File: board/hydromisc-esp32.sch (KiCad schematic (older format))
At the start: 53 parts, among them CN12 MOLEX_2x3, CN13 MOLEX_2x3, CN14 COAX_CONNECTOR, CN15 HEADER_6, CN16 MOLEX_2x2, CN3 COAX_CONNECTOR, CN4 MOLEX_2x2, IC2 74HC594, IC4 74HC594, IC5 opamp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

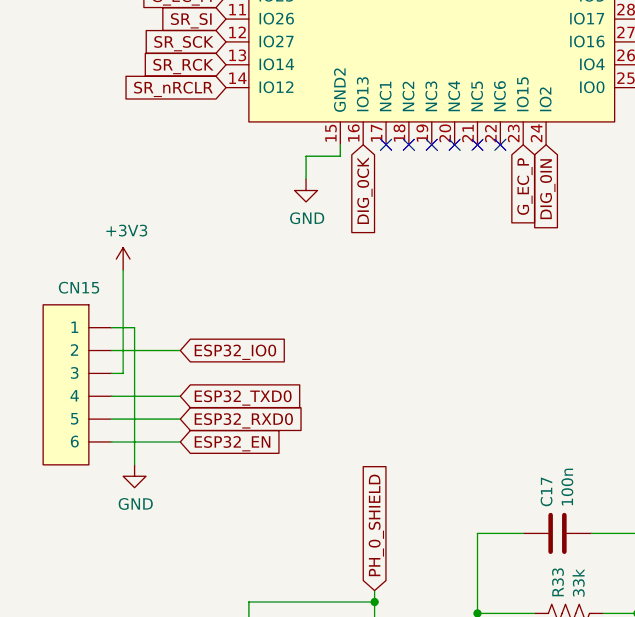
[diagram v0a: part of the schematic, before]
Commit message: Update PCB to rev B.
Add the missing pull-up on ESP32_EN, some pull-down on Vuser to
fight off-brand LM2596 leakage current, and a README.md explaining.
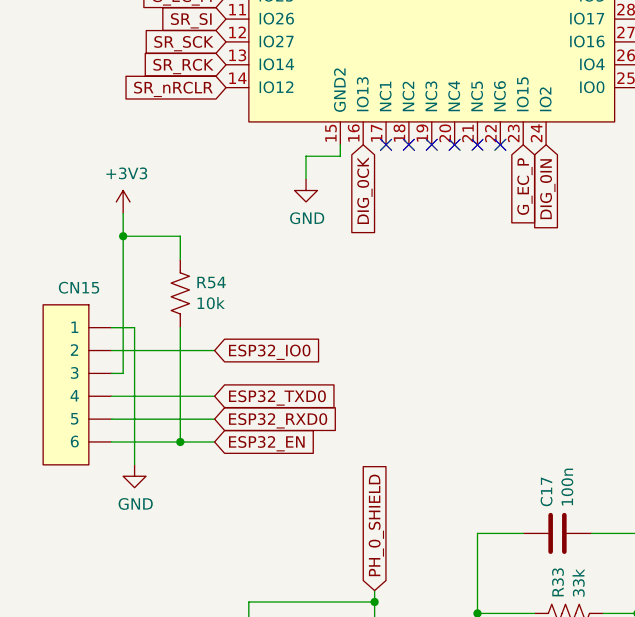
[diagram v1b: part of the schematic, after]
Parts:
- added R54: 10k, hydromisc:HM_0603, symbol Device:R_US
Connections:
- net +3V3: now also R54.1
- net ESP32_EN: now also R54.2
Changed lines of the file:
@@
 Wire Wire Line
 	1300 4100 1350 4100
-Wire Wire Line
-	1350 4100 1350 3650
 $Comp
 L power:+3V3 #PWR0125
 U 1 1 6114B426
-P 1350 3650
-F 0 "#PWR0125" H 1350 3500 50  0001 C CNN
-F 1 "+3V3" H 1365 3823 50  0000 C CNN
-F 2 "" H 1350 3650 50  0001 C CNN
-F 3 "" H 1350 3650 50  0001 C CNN
-	1    1350 3650
-	1    0    0    -1
-$EndComp
-Wire Wire Line
-	1600 4000 1300 4000
-Wire Wire Line
-	1600 4200 1300 4200
-Wire Wire Line
-	1600 4300 1300 4300
-Wire Wire Line
-	1600 4400 1300 4400
-Text GLabel 1600 4000 2    50   Input ~ 0
+P 1350 3400
+F 0 "#PWR0125" H 1350 3250 50  0001 C CNN
+F 1 "+3V3" H 1365 3573 50  0000 C CNN
+F 2 "" H 1350 3400 50  0001 C CNN
+F 3 "" H 1350 3400 50  0001 C CNN
+	1    1350 3400
+	1    0    0    -1
+$EndComp
+Text GLabel 1750 4000 2    50   Input ~ 0
 ESP32_IO0
-Text GLabel 1600 4200 2    50   Input ~ 0
+Text GLabel 1750 4200 2    50   Input ~ 0
 ESP32_TXD0
-Text GLabel 1600 4300 2    50   Input ~ 0
+Text GLabel 1750 4300 2    50   Input ~ 0
 ESP32_RXD0
-Text GLabel 1600 4400 2    50   Input ~ 0
+Text GLabel 1750 4400 2    50   Input ~ 0
 ESP32_EN
 Text GLabel 1800 2450 0    50   Input ~ 0
@@
 Wire Wire Line
 	2450 6600 2450 6900
+$Comp
+L Device:R_US R?
+U 1 1 60E2809B
+P 1600 3750
+AR Path="/6036C67E/60E2809B" Ref="R?"  Part="1"
+AR Path="/603346A0/60E2809B" Ref="R54"  Part="1"
+F 0 "R54" H 1668 3796 50  0000 L CNN
+F 1 "10k" H 1668 3705 50  0000 L CNN
+F 2 "hydromisc:HM_0603" V 1640 3740 50  0001 C CNN
+F 3 "~" H 1600 3750 50  0001 C CNN
+	1    1600 3750
+	1    0    0    -1
+$EndComp
+Wire Wire Line
+	1300 4000 1750 4000
+Wire Wire Line
+	1300 4200 1750 4200
+Wire Wire Line
+	1300 4300 1750 4300
+Wire Wire Line
+	1300 4400 1600 4400
+Wire Wire Line
+	1600 3900 1600 4400
+Connection ~ 1600 4400
+Wire Wire Line
+	1600 4400 1750 4400
+Wire Wire Line
+	1600 3600 1600 3500
+Wire Wire Line
+	1600 3500 1350 3500
+Connection ~ 1350 3500
+Wire Wire Line
+	1350 3500 1350 4100
+Wire Wire Line
+	1350 3400 1350 3500
 $EndSCHEMATC

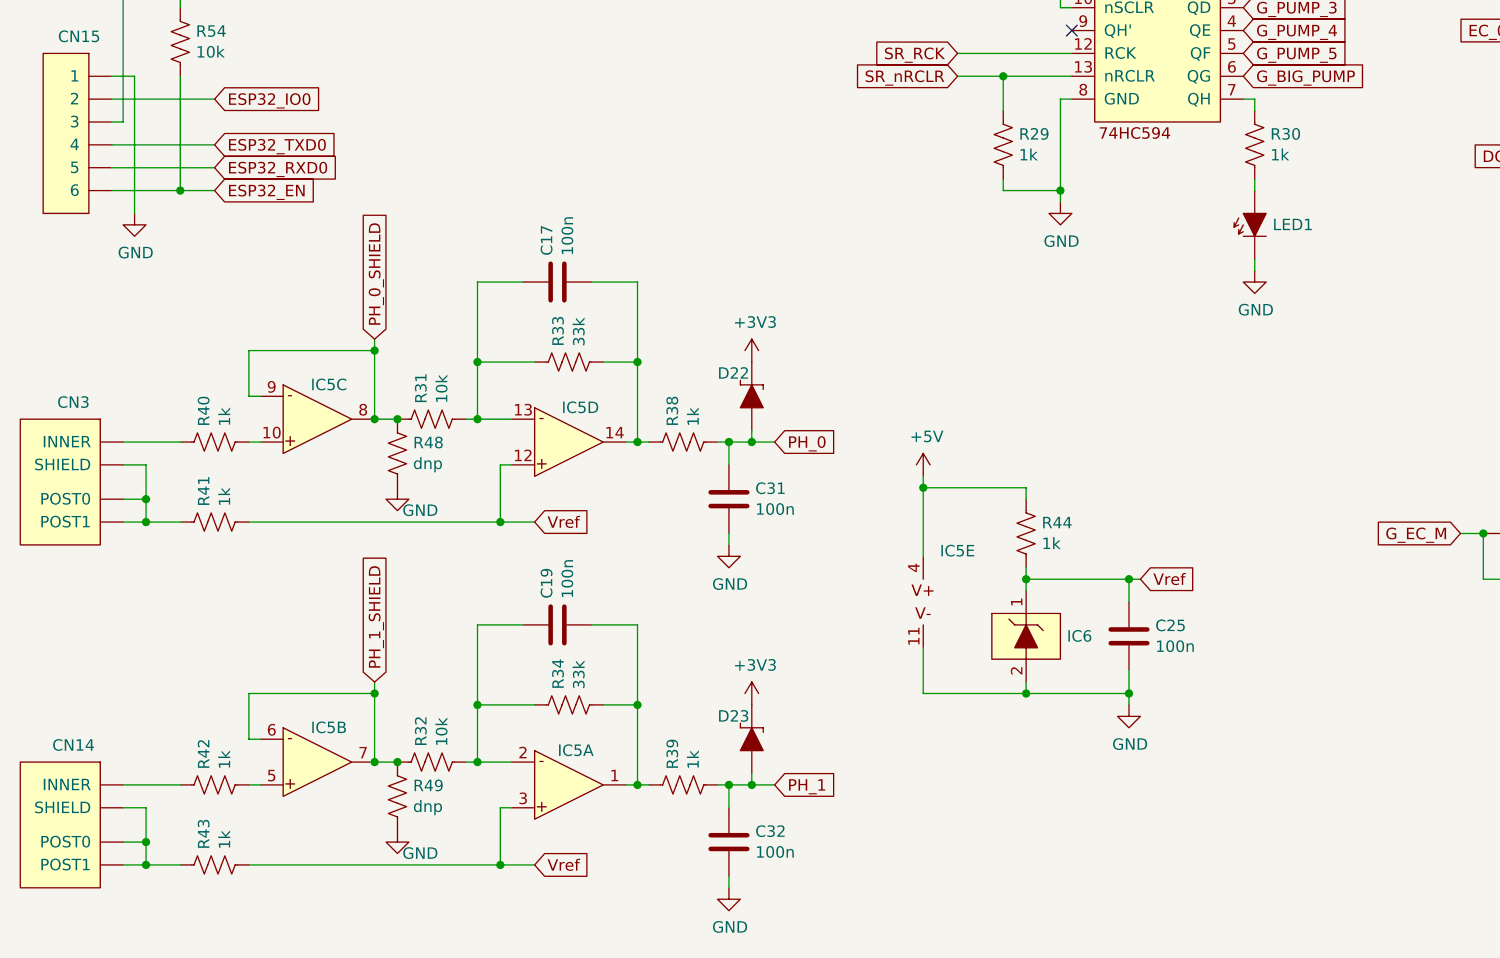
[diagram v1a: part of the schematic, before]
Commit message: Add capacitors directly across pH probes.
This fixes a problem with 60 Hz (or 50 Hz) pickup, when the wires are
long or the noise is coupling to the water. Also replace the 1k resistors
to the shield with zero-ohm resistors, to further reduce that noise.

This updates the board to rev C. Also check in PDF schematics, BOM,
and Gerbers.
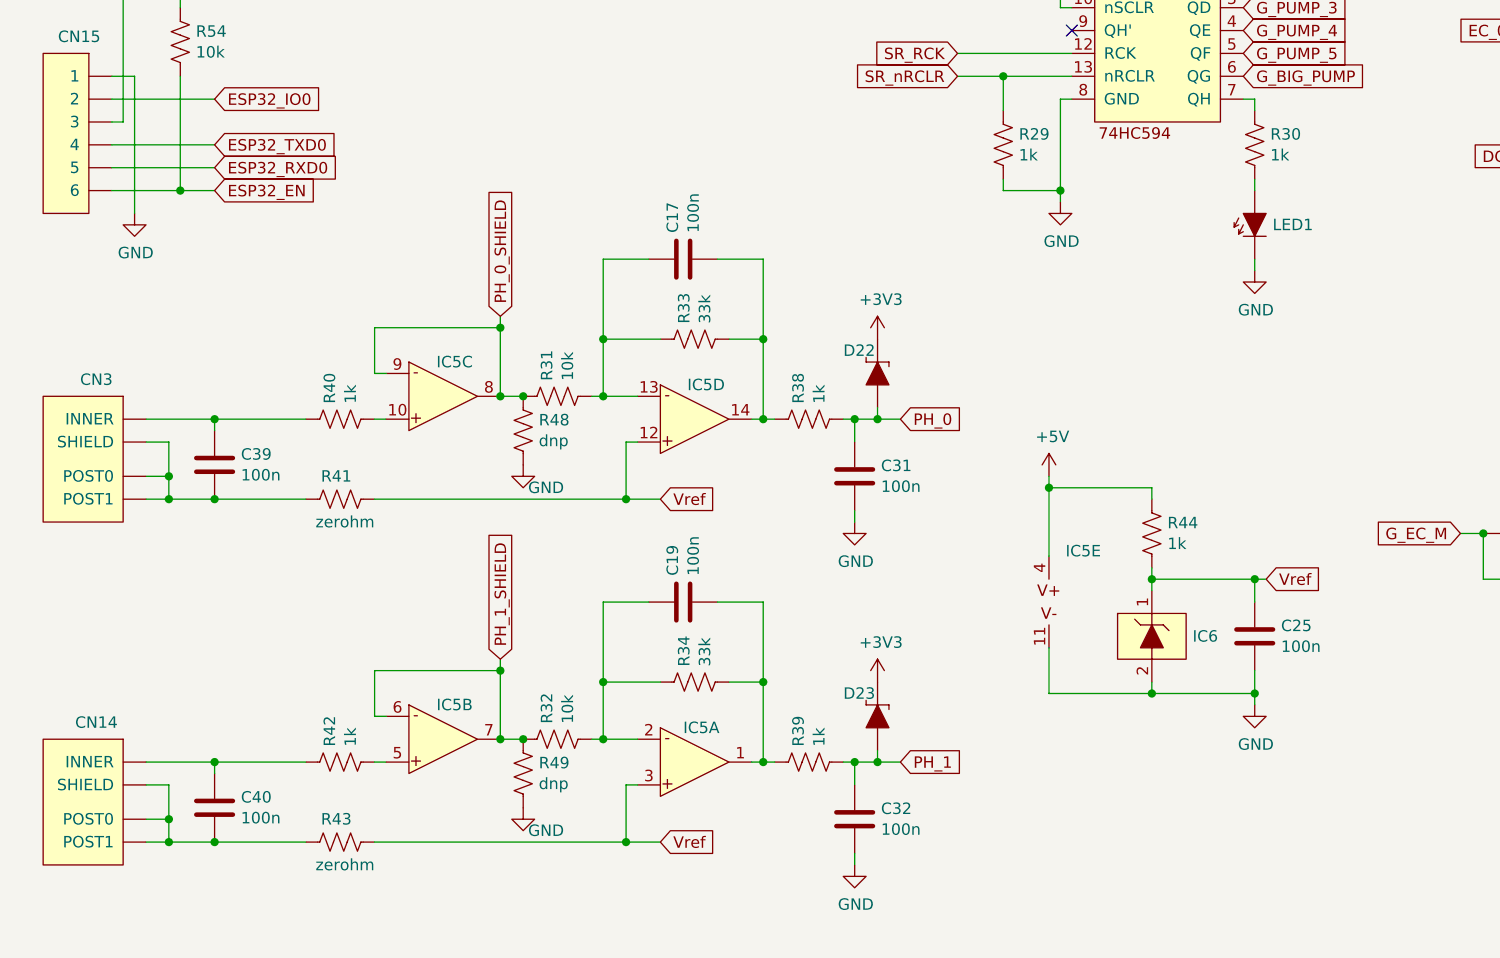
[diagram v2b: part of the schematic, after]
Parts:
- added C39, C40: 100n, hydromisc:HM_0603, symbol Device:C
- R41, R43: value 1k -> zerohm
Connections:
- net at CN3.INNER, R40.1: now also C39.1
- net at CN3.POST0, CN3.POST1, CN3.SHIELD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: now also C39.2
- net at CN14.INNER, R42.1: now also C40.1
- net at CN14.POST0, CN14.POST1, CN14.SHIELD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: now also C40.2
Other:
- moved on the sheet: C17, C19, C25, C31, C32, CN14, CN3, D22, D23, IC5A, IC5B, IC5C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
